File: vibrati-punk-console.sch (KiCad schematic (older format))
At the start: 22 parts, among them J1 Conn_01x02_Male, J2 Conn_01x02_Male, U1 NE555, U2 NE555, U3 NE555

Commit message: Don't know what really change, but the schematics looks good ;d
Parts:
- added SW?: SW_DPST, symbol Switch:SW_DPST
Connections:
- net +9V: now also SW?.4; no longer C7.1, C8.1
- net GND: now also SW?.2
- new net: C7.1, C8.1, SW?.3
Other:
- moved on the sheet: C7, C8
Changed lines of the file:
@@
-$EndComp
-$Comp
-L power:GND #PWR?
-U 1 1 5D7ADD2F
-P 10600 1100
-F 0 "#PWR?" H 10600 850 50  0001 C CNN
-F 1 "GND" H 10605 927 50  0000 C CNN
-F 2 "" H 10600 1100 50  0001 C CNN
-F 3 "" H 10600 1100 50  0001 C CNN
-	1    10600 1100
-	0    -1   -1   0
-$EndComp
-$Comp
-L Device:C C8
-U 1 1 5D7D30E9
-P 10300 950
-F 0 "C8" H 10415 996 50  0000 L CNN
-F 1 "100n" H 10415 905 50  0000 L CNN
-F 2 "" H 10338 800 50  0001 C CNN
-F 3 "~" H 10300 950 50  0001 C CNN
-	1    10300 950
-	1    0    0    -1
-$EndComp
-$Comp
-L Device:C C7
-U 1 1 5D7D358B
-P 9800 950
-F 0 "C7" H 9915 996 50  0000 L CNN
-F 1 "100n" H 9915 905 50  0000 L CNN
-F 2 "" H 9838 800 50  0001 C CNN
-F 3 "~" H 9800 950 50  0001 C CNN
-	1    9800 950
-	1    0    0    -1
 $EndComp
 $Comp
@@
 	1    0    0    -1
 $EndComp
-Wire Wire Line
-	10300 750  10300 800
-Wire Wire Line
-	9800 1100 10300 1100
-Connection ~ 10300 1100
-Wire Wire Line
-	10300 1100 10600 1100
-Wire Wire Line
-	9800 750  9800 800
-Wire Wire Line
-	9800 750  10300 750
-Wire Wire Line
-	10600 750  10300 750
-Connection ~ 10300 750
 Wire Wire Line
 	10400 1650 10150 1650
@@
 Wire Wire Line
 	4350 2000 4350 2050
+$Comp
+L Switch:SW_DPST SW?
+U 1 1 5D9AE21B
+P 9350 1000
+F 0 "SW?" H 9350 1325 50  0000 C CNN
+F 1 "SW_DPST" H 9350 1234 50  0000 C CNN
+F 2 "" H 9350 1000 50  0001 C CNN
+F 3 "~" H 9350 1000 50  0001 C CNN
+	1    9350 1000
+	1    0    0    -1
+$EndComp
+$Comp
+L Device:C C7
+U 1 1 5D7D358B
+P 9800 1050
+F 0 "C7" H 9915 1096 50  0000 L CNN
+F 1 "100n" H 9915 1005 50  0000 L CNN
+F 2 "" H 9838 900 50  0001 C CNN
+F 3 "~" H 9800 1050 50  0001 C CNN
+	1    9800 1050
+	1    0    0    -1
+$EndComp
+Wire Wire Line
+	10300 850  10300 950
+Connection ~ 10300 1250
+Wire Wire Line
+	9800 1250 10300 1250
+$Comp
+L Device:C C8
+U 1 1 5D7D30E9
+P 10300 1100
+F 0 "C8" H 10415 1146 50  0000 L CNN
+F 1 "100n" H 10415 1055 50  0000 L CNN
+F 2 "" H 10338 950 50  0001 C CNN
+F 3 "~" H 10300 1100 50  0001 C CNN
+	1    10300 1100
+	1    0    0    -1
+$EndComp
+$Comp
+L power:GND #PWR?
+U 1 1 5D7ADD2F
+P 10600 1250
+F 0 "#PWR?" H 10600 1000 50  0001 C CNN
+F 1 "GND" H 10605 1077 50  0000 C CNN
+F 2 "" H 10600 1250 50  0001 C CNN
+F 3 "" H 10600 1250 50  0001 C CNN
+	1    10600 1250
+	0    -1   -1   0
+$EndComp
+Wire Wire Line
+	10300 1250 10600 1250
+Wire Wire Line
+	9800 1200 9800 1250
+Wire Wire Line
+	10600 750  9550 750
+Wire Wire Line
+	9550 750  9550 900
+Wire Wire Line
+	9150 900  9150 600
+Wire Wire Line
+	9150 600  9800 600
+Wire Wire Line
+	9800 600  9800 850
+Wire Wire Line
+	9800 850  10300 850
+Connection ~ 9800 850
+Wire Wire Line
+	9800 850  9800 900
+Wire Wire Line
+	9550 1100 9550 1250
+Wire Wire Line
+	9550 1250 9800 1250
+Connection ~ 9800 1250
 $EndSCHEMATC

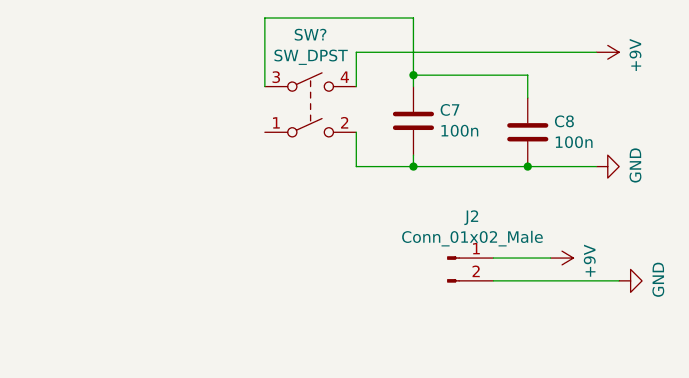
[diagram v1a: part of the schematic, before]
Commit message: Untangle main power source
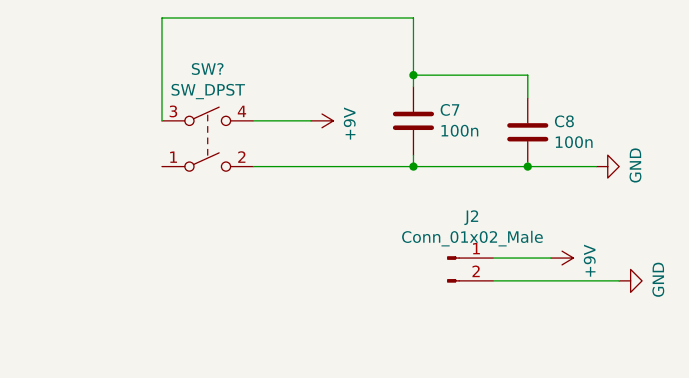
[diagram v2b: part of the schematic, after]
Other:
- moved on the sheet: SW?
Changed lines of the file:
@@
-$Comp
-L power:+9V #PWR?
-U 1 1 5D7ACB0A
-P 10600 750
-F 0 "#PWR?" H 10600 600 50  0001 C CNN
-F 1 "+9V" H 10615 923 50  0000 C CNN
-F 2 "" H 10600 750 50  0001 C CNN
-F 3 "" H 10600 750 50  0001 C CNN
-	1    10600 750
-	0    1    1    0
-$EndComp
 $Comp
 L power:+9V #PWR?
@@
 	4350 2000 4350 2050
 $Comp
-L Switch:SW_DPST SW?
-U 1 1 5D9AE21B
-P 9350 1000
-F 0 "SW?" H 9350 1325 50  0000 C CNN
-F 1 "SW_DPST" H 9350 1234 50  0000 C CNN
-F 2 "" H 9350 1000 50  0001 C CNN
-F 3 "~" H 9350 1000 50  0001 C CNN
-	1    9350 1000
-	1    0    0    -1
-$EndComp
-$Comp
 L Device:C C7
 U 1 1 5D7D358B
@@
 	9800 1200 9800 1250
 Wire Wire Line
-	10600 750  9550 750
-Wire Wire Line
-	9550 750  9550 900
-Wire Wire Line
-	9150 900  9150 600
-Wire Wire Line
-	9150 600  9800 600
-Wire Wire Line
 	9800 600  9800 850
 Wire Wire Line
@@
 Wire Wire Line
 	9800 850  9800 900
-Wire Wire Line
-	9550 1100 9550 1250
-Wire Wire Line
-	9550 1250 9800 1250
 Connection ~ 9800 1250
+$Comp
+L Switch:SW_DPST SW?
+U 1 1 5D9AE21B
+P 8900 1150
+F 0 "SW?" H 8900 1475 50  0000 C CNN
+F 1 "SW_DPST" H 8900 1384 50  0000 C CNN
+F 2 "" H 8900 1150 50  0001 C CNN
+F 3 "~" H 8900 1150 50  0001 C CNN
+	1    8900 1150
+	1    0    0    -1
+$EndComp
+Wire Wire Line
+	8700 600  9800 600
+$Comp
+L power:+9V #PWR?
+U 1 1 5D7ACB0A
+P 9350 1050
+F 0 "#PWR?" H 9350 900 50  0001 C CNN
+F 1 "+9V" H 9365 1223 50  0000 C CNN
+F 2 "" H 9350 1050 50  0001 C CNN
+F 3 "" H 9350 1050 50  0001 C CNN
+	1    9350 1050
+	0    1    1    0
+$EndComp
+Wire Wire Line
+	8700 600  8700 1050
+Wire Wire Line
+	9100 1250 9800 1250
+Wire Wire Line
+	9350 1050 9100 1050
 $EndSCHEMATC

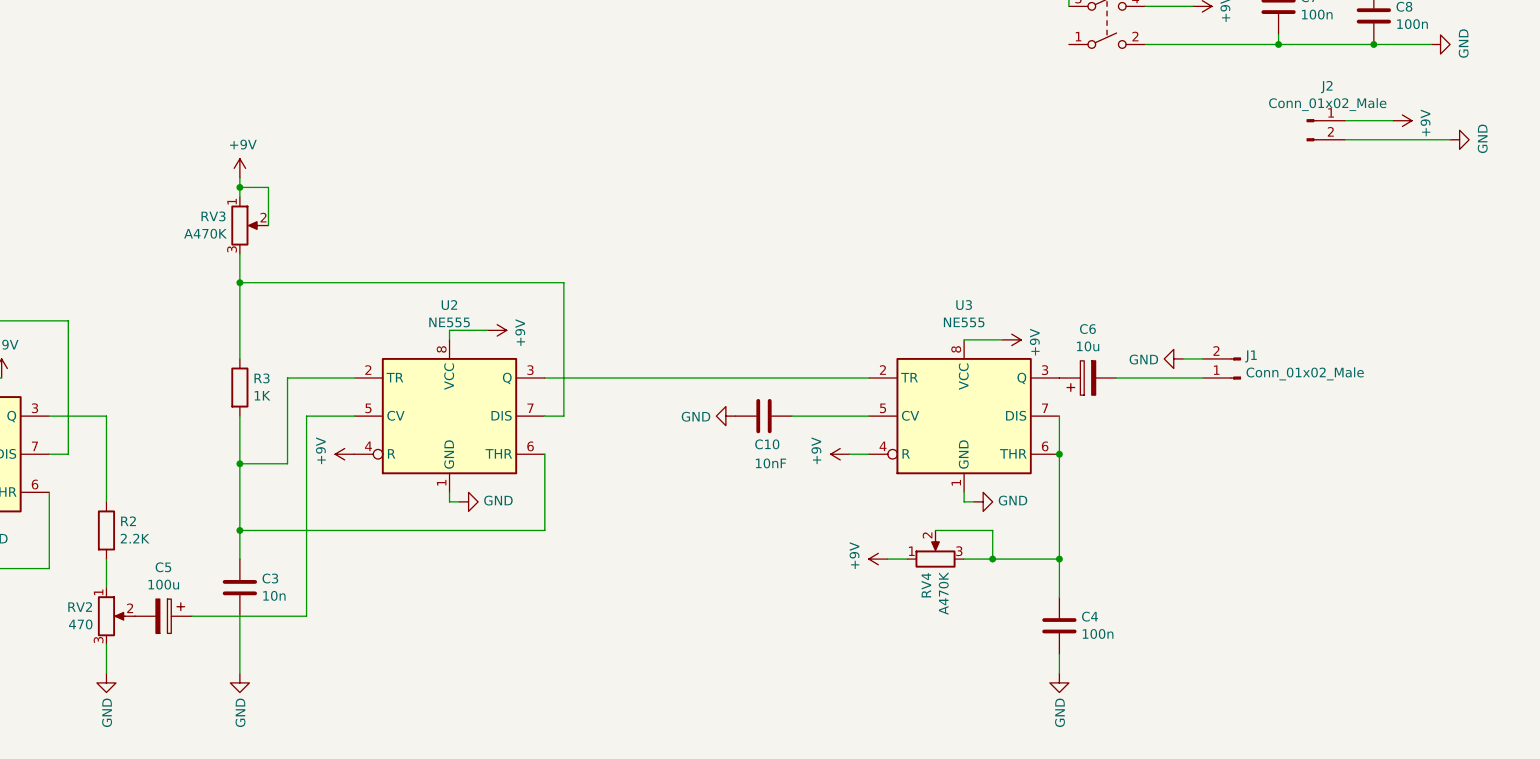
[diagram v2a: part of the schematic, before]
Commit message: Untangle GND over U2
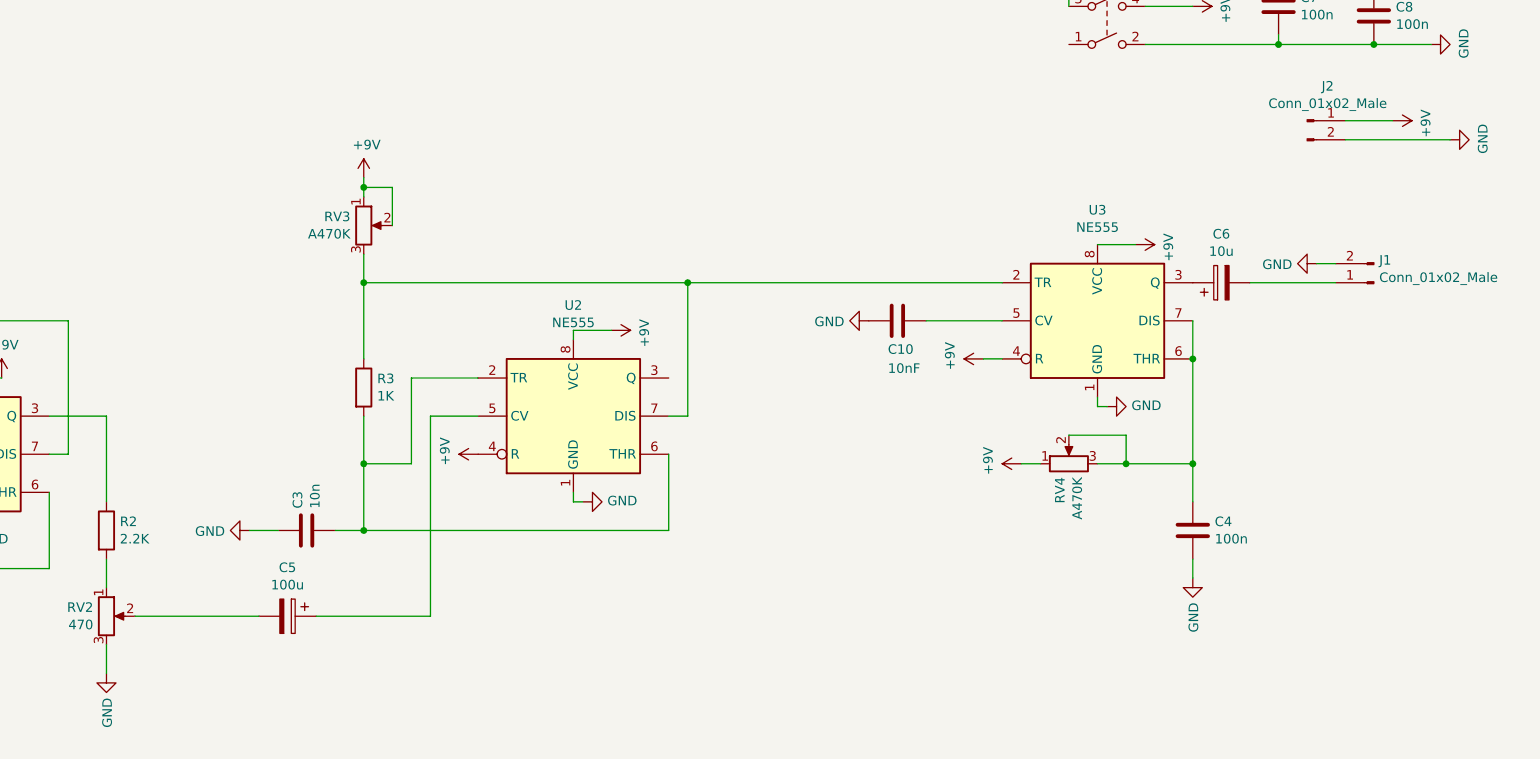
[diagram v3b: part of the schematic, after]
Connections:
- net GND: now also C3.1; no longer C3.2
- net at R3.2, U2.2 (TR), U2.6 (THR): now also C3.2; no longer C3.1
- net at U2.3 (Q): no longer U3.2 (TR)
- net at R3.1, RV3.3, U2.7 (DIS): now also U3.2 (TR)
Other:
- moved on the sheet: C10, C3, C4, C5, C6, J1, R3, RV3, RV4, U2, U3

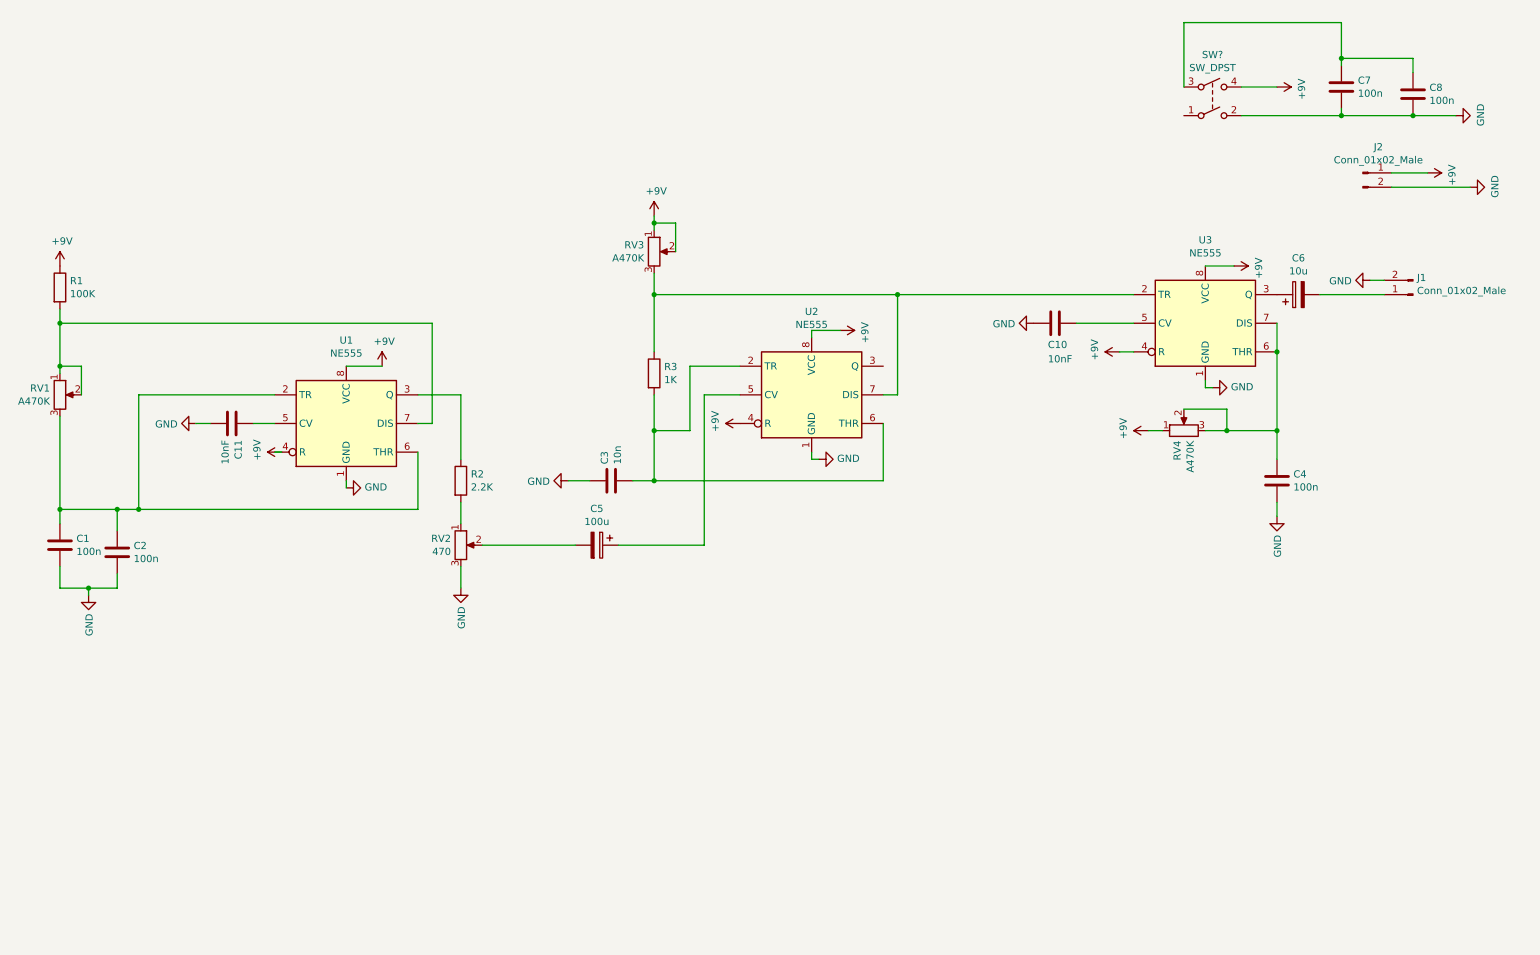
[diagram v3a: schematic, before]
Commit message: Make ground face down and power up
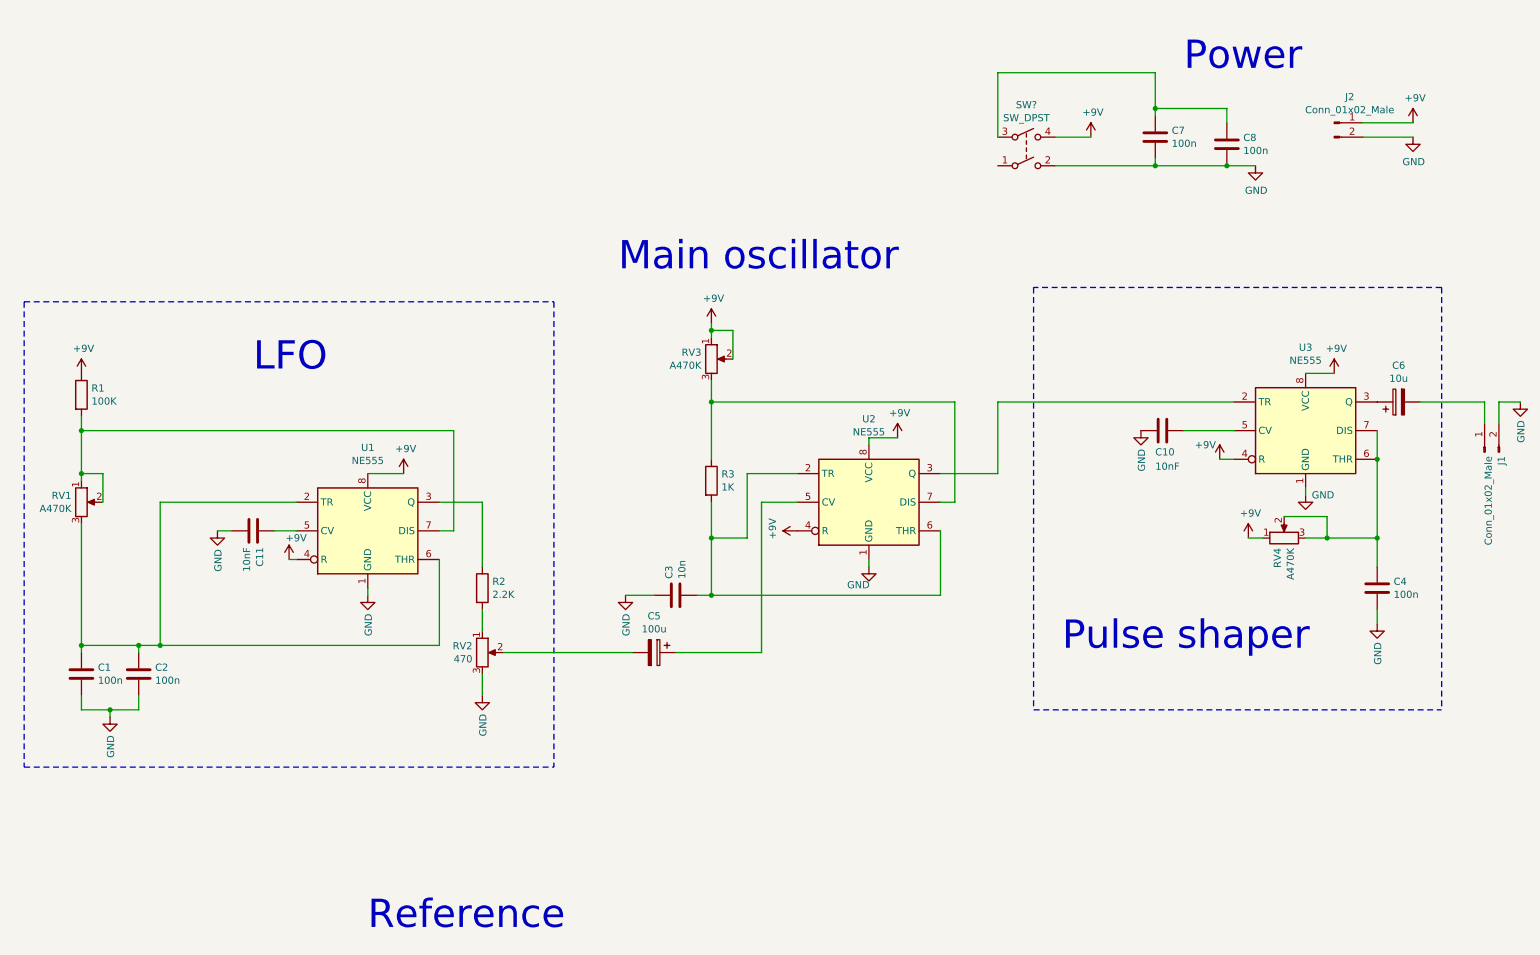
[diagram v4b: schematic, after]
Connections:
- net at U2.3 (Q): now also U3.2 (TR)
- net at R3.1, RV3.3, U2.7 (DIS): no longer U3.2 (TR)
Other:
- note added: "LFO"
- note added: "Main oscillator\n"
- note added: "Power"
- note added: "Pulse shaper"
- note added: "Reference"
- moved on the sheet: C1, C10, C11, C2, C3, C4, C5, C6, C7, C8, J1, J2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

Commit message: Move power decoupling closer to ICs
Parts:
- removed SW?: SW_DPST, symbol Switch:SW_DPST
- added C9: 100n, symbol Device:C
- added SW1: SW_SPST, symbol Switch:SW_SPST
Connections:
- net +9V: now also C7.2, C8.1, C9.2, SW1.2 (B); no longer J2.1 (Pin_1)
- net GND: now also C7.1, C9.1; no longer C7.2
- new net: J2.1 (Pin_1), SW1.1 (A)
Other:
- moved on the sheet: C7, C8, J2, RV3

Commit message: Unify capacitor values
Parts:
- C10, C11: value 10nF -> 10n
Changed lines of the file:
@@
 P 2200 4150
 F 0 "C11" H 2315 4196 50  0000 L CNN
-F 1 "10nF" H 2315 4105 50  0000 L CNN
+F 1 "10n" H 2315 4105 50  0000 L CNN
 F 2 "" H 2238 4000 50  0001 C CNN
 F 3 "~" H 2200 4150 50  0001 C CNN
@@
 Wire Wire Line
 	9700 4050 9700 4200
-Wire Wire Line
-	9150 4200 9250 4200
 $Comp
 L power:GND #PWR?
@@
 $EndComp
 $Comp
-L power:+9V #PWR?
-U 1 1 5D8F8F10
-P 9150 4200
-F 0 "#PWR?" H 9150 4050 50  0001 C CNN
-F 1 "+9V" H 9165 4373 50  0000 C CNN
-F 2 "" H 9150 4200 50  0001 C CNN
-F 3 "" H 9150 4200 50  0001 C CNN
-	1    9150 4200
-	1    0    0    -1
-$EndComp
-$Comp
 L Device:C C10
 U 1 1 5D82E5E1
 P 8550 3450
 F 0 "C10" V 8700 3400 50  0000 L CNN
-F 1 "10nF" V 8800 3400 50  0000 L CNN
+F 1 "10n" V 8800 3400 50  0000 L CNN
 F 2 "" H 8588 3300 50  0001 C CNN
 F 3 "~" H 8550 3450 50  0001 C CNN
@@
 Wire Notes Line
 	10500 2350 10500 5400
+Wire Wire Line
+	9150 4200 9250 4200
+$Comp
+L power:+9V #PWR?
+U 1 1 5D8F8F10
+P 9150 4200
+F 0 "#PWR?" H 9150 4050 50  0001 C CNN
+F 1 "+9V" H 9165 4373 50  0000 C CNN
+F 2 "" H 9150 4200 50  0001 C CNN
+F 3 "" H 9150 4200 50  0001 C CNN
+	1    9150 4200
+	1    0    0    -1
+$EndComp
 $EndSCHEMATC
